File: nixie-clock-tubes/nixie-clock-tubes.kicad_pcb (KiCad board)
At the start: 2 copper layers, 134 x 33 mm, 23 parts, among them J1 Conn_02x05_Odd_Even, J2 Conn_02x05_Odd_Even, J3 Conn_02x05_Odd_Even, J4 Conn_02x05_Odd_Even, J5 Conn_02x05_Odd_Even, J6 Conn_02x05_Odd_Even, J7 Conn_02x02_Odd_Even

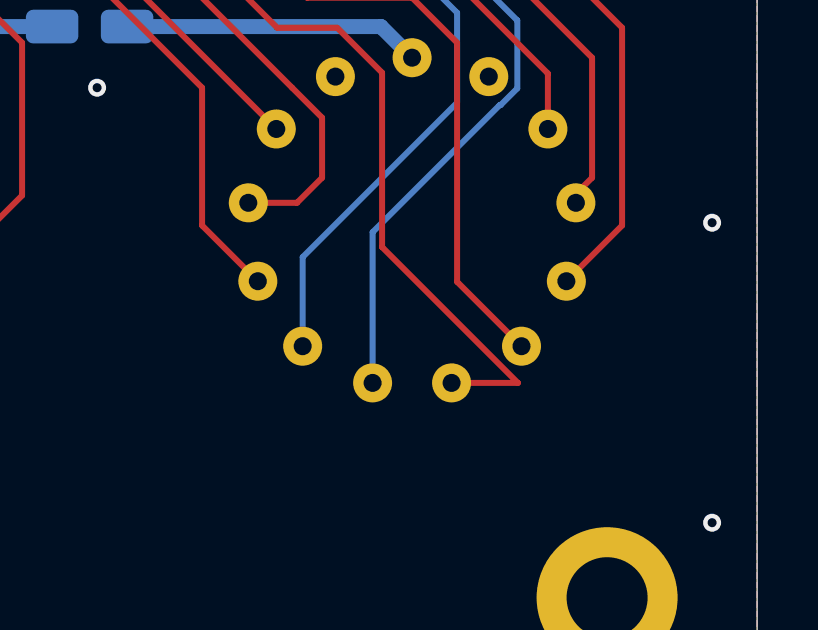
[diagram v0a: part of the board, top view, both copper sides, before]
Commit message: nixie-clock-tubes: Fix small layout issue
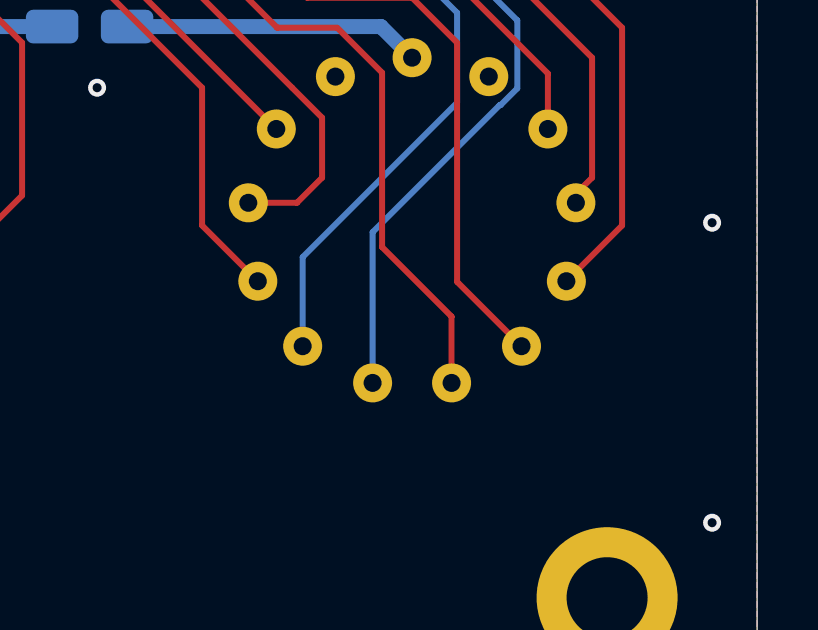
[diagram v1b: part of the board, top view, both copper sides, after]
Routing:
- net D6-5: track 28.0 -> 24.9 mm
